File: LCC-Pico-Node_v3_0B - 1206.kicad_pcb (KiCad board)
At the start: 4 copper layers, 100 x 82 mm, 89 parts, among them IC1 TPS54228DR, IC2 MCP2518FD, IC3 MCP2562FD, IC5 MB85RCxxxV, IC6 TPS54228DR, J1 RJ45, J12 Power Sel, J15 Analog I/O, J16 NVM Power Sel, J2 RJ45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

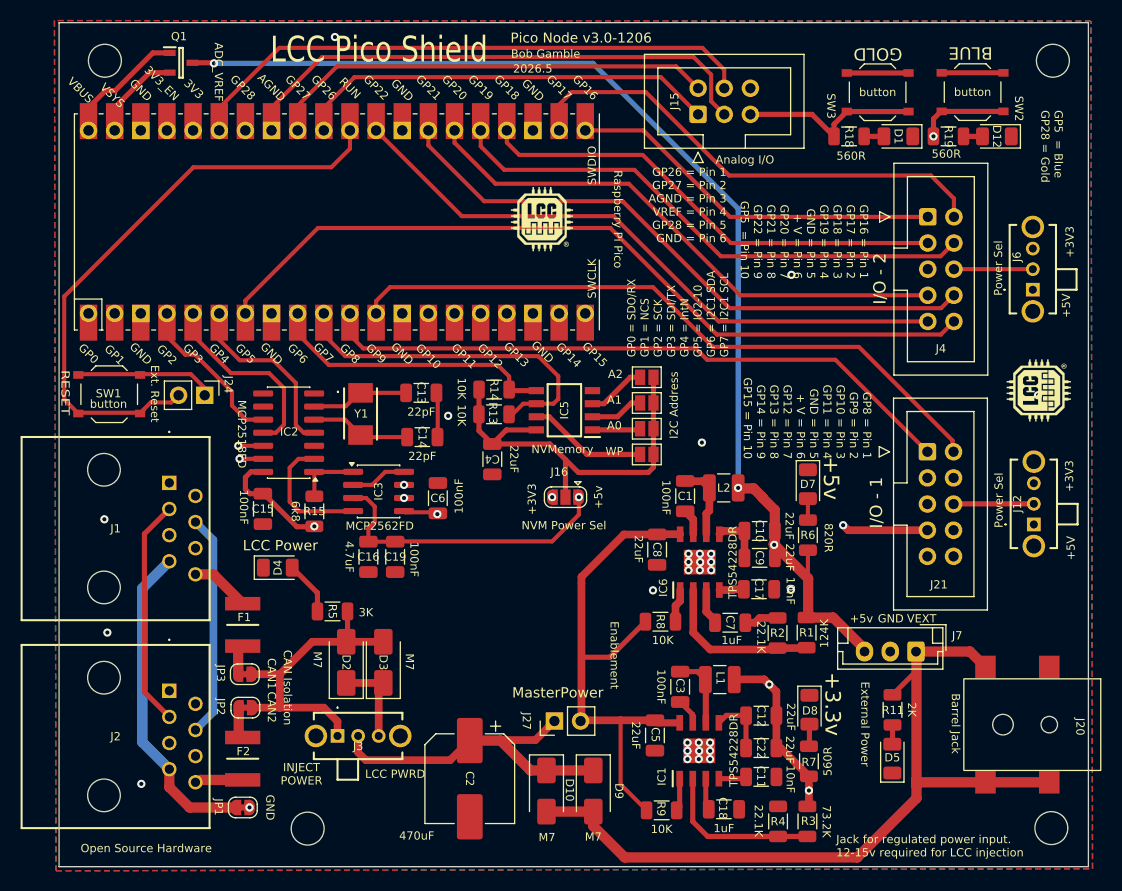
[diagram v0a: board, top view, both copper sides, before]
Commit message: Production level
0805 boards can be assembled at JLCPCB with these files
1206 boards are for hand assembly
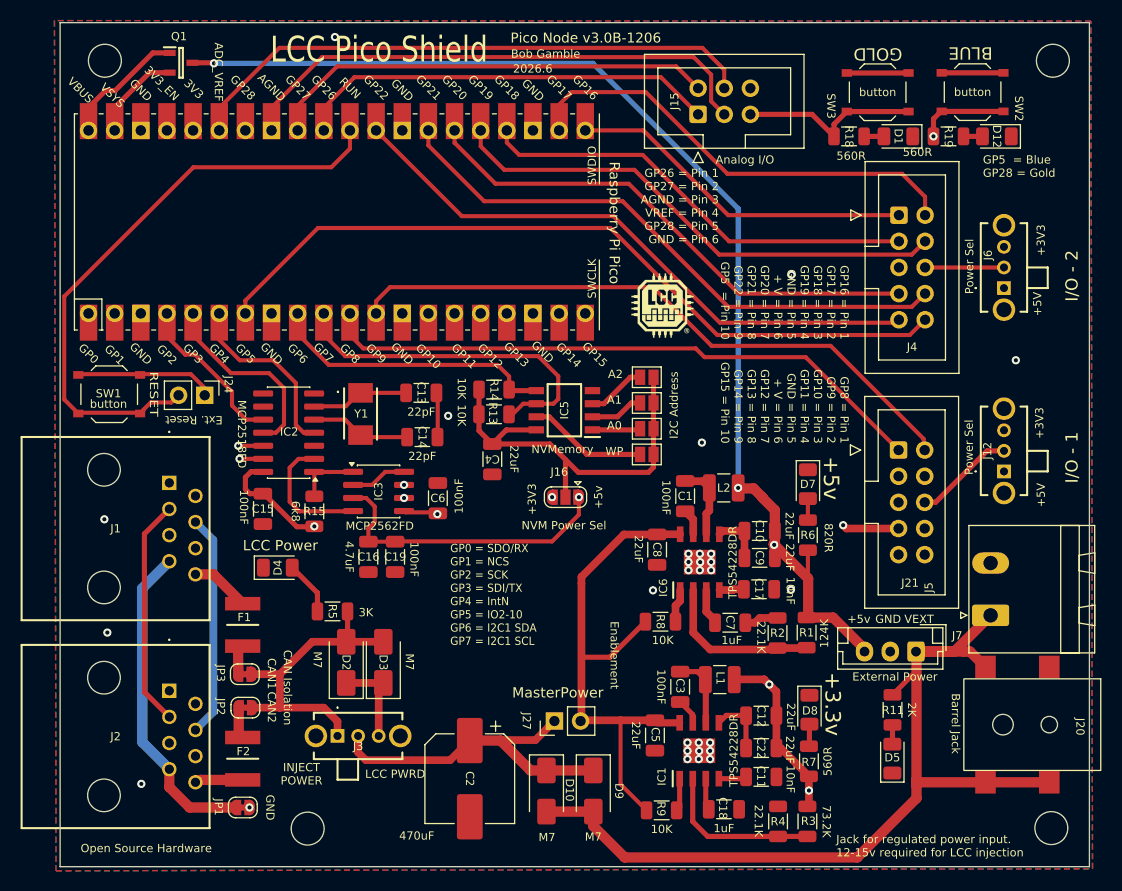
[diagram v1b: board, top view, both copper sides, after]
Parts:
- removed the G*** at (146.9, 69.0)
- added J5: External Power, Connector_Phoenix_MSTB:PhoenixContact_MSTBA_2,5_2-G-5,08_1x02_P5.08mm_Horizontal, F.Cu at (190.5, 107.6)
- moved G*** 37.4 mm to (158.7, 77.5), turned to 0 degrees
- moved J12 5.91 mm to (191.8, 93.6)
- moved J4 2.81 mm to (181.6, 68.7)
- moved J21 2.81 mm to (181.6, 91.5)
- moved J6 2.81 mm to (191.8, 75.8)
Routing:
- net VEXT: track 81.4 -> 90.1 mm
- net GP5: track 107.9 -> 103.9 mm
- net GP13: track 64.7 -> 61.7 mm
- net GP11: track 61.8 -> 58.8 mm
- net GP15: track 57.3 -> 54.2 mm
- net SDA0: track 36.8 -> 33.9 mm
- net GP18: track 46.6 -> 43.7 mm
- net GP12: track 54.5 -> 51.6 mm
- net GP20: track 53.3 -> 50.4 mm
- net SCL0: track 47.4 -> 44.6 mm
- net GP9: track 65.1 -> 62.3 mm
- net GP19: track 53.2 -> 50.3 mm
- net GP8: track 62.9 -> 60.0 mm
- net GP21: track 59.6 -> 56.7 mm
- net GP10: track 56.8 -> 54.0 mm
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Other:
- board text added: "2026.6"
- board text added: "May be configured for zero LCC draw or to draw Pico processor and attachment power from LCC May draw from both external source and LCC May inject power to LCC with proper external power"
- board text added: "Pico Node v3.0B"
- board text added: "Pico Node v3.0B-1206"
- board text removed: "2026.5"
- board text removed: "May be configured for zero LCC draw or to draw Pico processor and attachment power from LCC May draw from both barrel jack and LCC May inject power to LCC with proper external power"
- board text removed: "Pico Node v3.0"
- board text removed: "Pico Node v3.0-1206"
